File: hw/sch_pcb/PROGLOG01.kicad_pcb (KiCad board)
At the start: 2 copper layers, 60.5 x 40.1 mm, 66 parts, among them J1 JUMP_3X2, J10 HEADER_2x01_PARALLEL, J11 HEADER_2x01_PARALLEL, J13 HEADER_2x01_PARALLEL, J14 HEADER_2x01_PARALLEL, J15 HEADER_2x01_PARALLEL, J16 HEADER_2x01_PARALLEL, J17 HEADER_2x01_PARALLEL, J18 HEADER_2x01_PARALLEL, J19 HEADER_2x01_PARALLEL, J2 HEADER_2x01, J20 HEADER_2x01_PARALLEL, J21 HEADER_2x01_PARALLEL, J22 HEADER_2x01_PARALLEL, J23 HEADER_2x01_PARALLEL, J24 HEADER_2x01_PARALLEL, J25 HEADER_2x01_PARALLEL, J26 SATA, J27 HEADER_2x01_PARALLEL, J28 HEADER_2x01_PARALLEL, J29 HEADER_2x01_PARALLEL, J3 HEADER_2x02_PARALLEL, J30 HEADER_2x01_PARALLEL, J31 HEADER_2x01_PARALLEL, J32 HEADER_2x01_PARALLEL, J33 HEADER_2x01_PARALLEL, J34 HEADER_2x01_PARALLEL, J4 HEADER_2x04, J5 HEADER_2x01_PARALLEL, J6 HEADER_2x01_PARALLEL, J7 HEADER_2x01_PARALLEL, J8 HEADER_2x01_PARALLEL, J9 HEADER_2x01_PARALLEL, M1 HOLE, M2 HOLE, M3 HOLE, M4 HOLE, SW1 SW_Push, U1 TPS22919DCK, U2 MIC5504-1.2YM5, U3 AT25SF081-SSH, U4 ICE40UP5K-SG48I, X1 ISM92-3351AH24.00

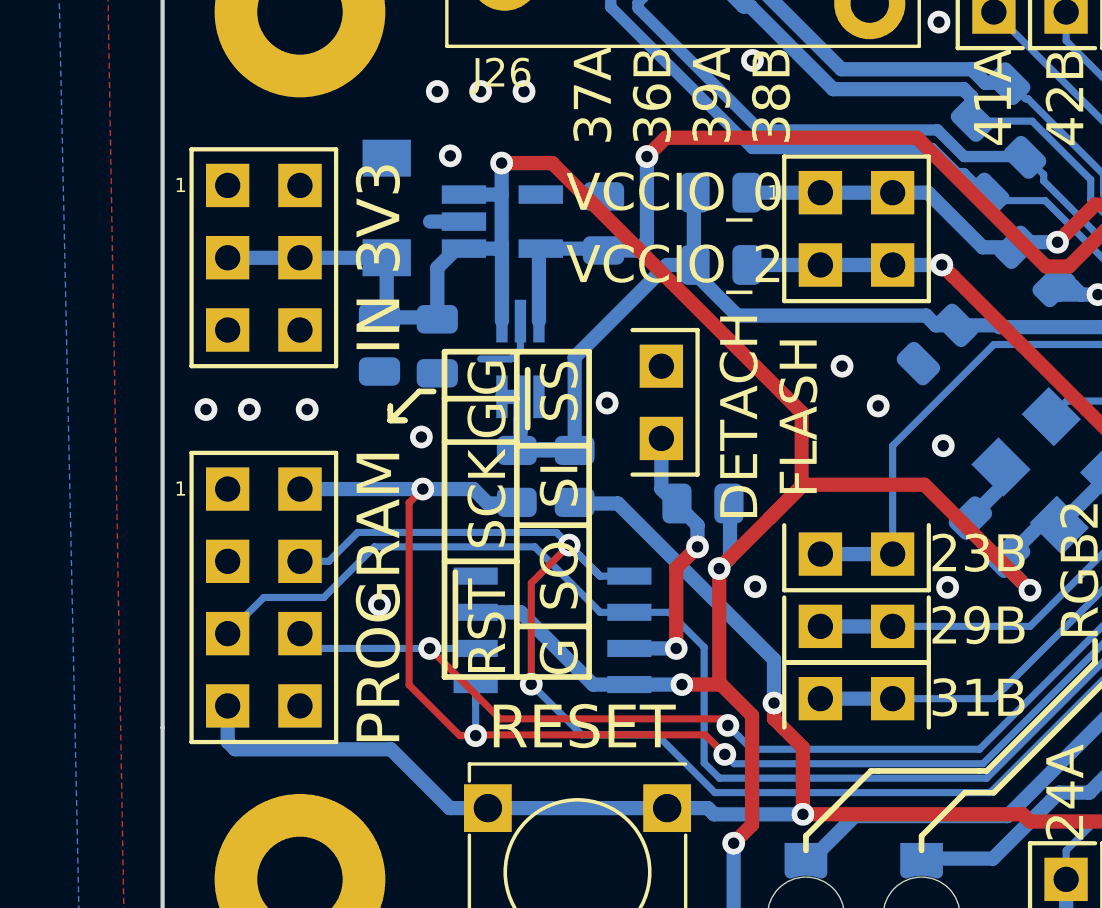
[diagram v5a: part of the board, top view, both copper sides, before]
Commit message: Resolve DRC errors in silkscreen.
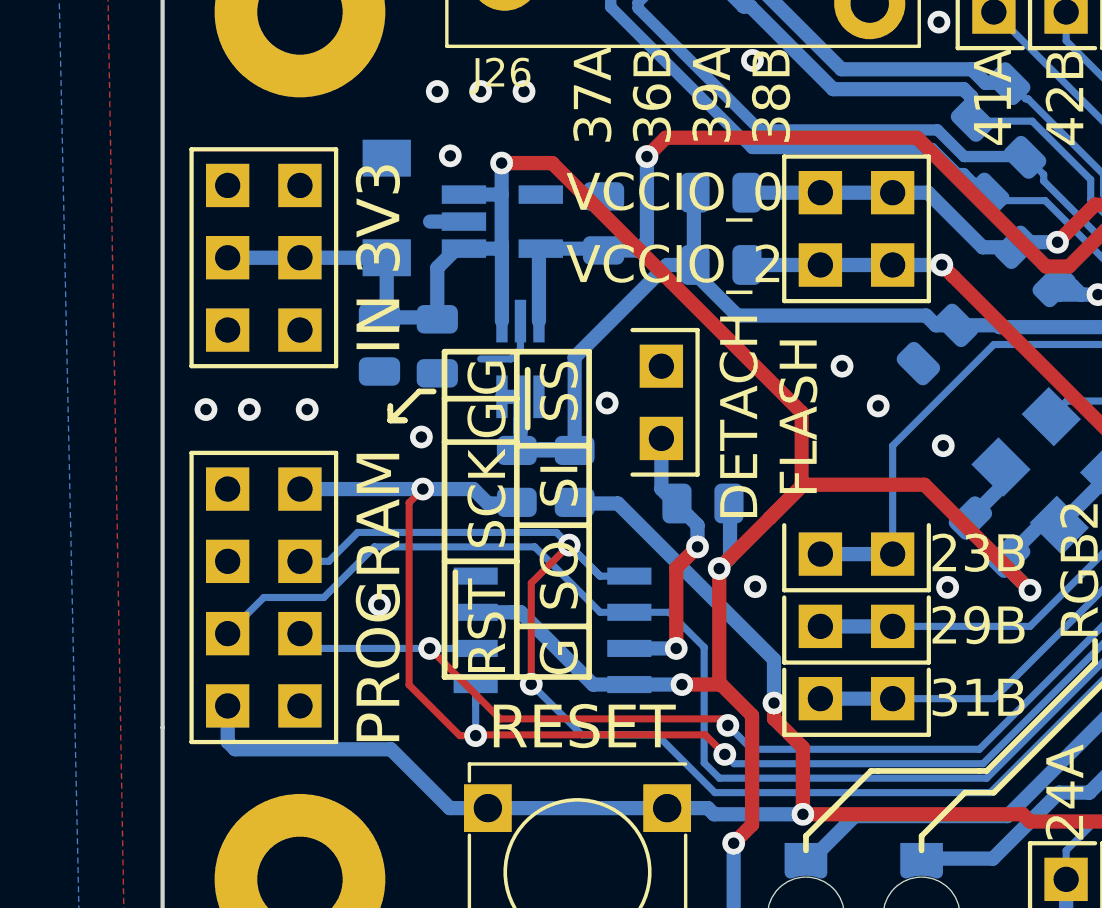
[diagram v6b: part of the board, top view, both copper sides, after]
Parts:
- turned J14 to 0 degrees
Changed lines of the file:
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@@
       (effects (font (size 1.5 1.5) (thickness 0.15)))
-    )
-    (fp_text user "1" (at -2.921 -2.54) (layer "F.SilkS")
-      (effects (font (size 0.5 0.5) (thickness 0.05)))
     )
     (fp_line (start 2.54 -3.81) (end 2.54 3.81) (layer "F.SilkS") (width 0.15))
@@
     (fp_text value "HEADER_2x04" (at 0 6.35) (layer "F.SilkS") hide
       (effects (font (size 1.5 1.5) (thickness 0.15)))
-    )
-    (fp_text user "1" (at -2.921 -3.81) (layer "F.SilkS")
-      (effects (font (size 0.5 0.5) (thickness 0.05)))
     )
     (fp_line (start -2.54 -5.08) (end 2.54 -5.08) (layer "F.SilkS") (width 0.15))
@@
   )
   (footprint "Mlab_Pin_Headers:Straight_2x01" (layer "F.Cu")
-    (at 181.864 130.556 180)
-    (descr "pin header straight 2x01")
-    (tags "pin header straight 2x01")
-    (property "Sheetfile" "PROGLOG01.kicad_sch")
-    (property "Sheetname" "")
-    (attr through_hole)
-    (fp_text reference "J14" (at 0 -2.54 180) (layer "F.SilkS") hide
-      (effects (font (size 1.5 1.5) (thickness 0.15)))
-    )
-    (fp_text value "HEADER_2x01_PARALLEL" (at 0 2.54 180) (layer "F.SilkS") hide
-      (effects (font (size 1.5 1.5) (thickness 0.15)))
-    )
-    (fp_line (start -2.54 1.27) (end -2.54 -1.016) (layer "F.SilkS") (width 0.15))
-    (fp_line (start 2.54 1.27) (end -2.54 1.27) (layer "F.SilkS") (width 0.15))
-    (fp_line (start 2.54 -1.016) (end 2.54 1.27) (layer "F.SilkS") (width 0.15))
-    (fp_line (start 2.54 1.27) (end -2.54 1.27) (layer "F.Fab") (width 0.15))
-    (fp_line (start 2.54 -1.27) (end 2.54 1.27) (layer "F.Fab") (width 0.15))
-    (fp_line (start -2.54 -1.27) (end 2.54 -1.27) (layer "F.Fab") (width 0.15))
-    (fp_line (start -2.54 1.27) (end -2.54 -1.27) (layer "F.Fab") (width 0.15))
-    (pad "1" thru_hole rect (at -1.27 0 180) (size 1.524 1.524) (drill 0.889) (layers *.Cu *.Mask)
+    (at 181.864 130.556)
+    (descr "pin header straight 2x01")
+    (tags "pin header straight 2x01")
+    (property "Sheetfile" "PROGLOG01.kicad_sch")
+    (property "Sheetname" "")
+    (attr through_hole)
+    (fp_text reference "J14" (at 0 -2.54) (layer "F.SilkS") hide
+      (effects (font (size 1.5 1.5) (thickness 0.15)))
+    )
+    (fp_text value "HEADER_2x01_PARALLEL" (at 0 2.54) (layer "F.SilkS") hide
+      (effects (font (size 1.5 1.5) (thickness 0.15)))
+    )
+    (fp_line (start -2.54 1.27) (end -2.54 -1.016) (layer "F.SilkS") (width 0.15))
+    (fp_line (start 2.54 1.27) (end -2.54 1.27) (layer "F.SilkS") (width 0.15))
+    (fp_line (start 2.54 -1.016) (end 2.54 1.27) (layer "F.SilkS") (width 0.15))
+    (fp_line (start 2.54 1.27) (end -2.54 1.27) (layer "F.Fab") (width 0.15))
+    (fp_line (start 2.54 -1.27) (end 2.54 1.27) (layer "F.Fab") (width 0.15))
+    (fp_line (start -2.54 -1.27) (end 2.54 -1.27) (layer "F.Fab") (width 0.15))
+    (fp_line (start -2.54 1.27) (end -2.54 -1.27) (layer "F.Fab") (width 0.15))
+    (pad "1" thru_hole rect (at -1.27 0) (size 1.524 1.524) (drill 0.889) (layers *.Cu *.Mask)
       (net 45 "/IOB_31b") (pintype "input"))
-    (pad "2" thru_hole rect (at 1.27 0 180) (size 1.524 1.524) (drill 0.889) (layers *.Cu *.Mask)
+    (pad "2" thru_hole rect (at 1.27 0) (size 1.524 1.524) (drill 0.889) (layers *.Cu *.Mask)
       (net 45 "/IOB_31b") (pintype "input"))
     (model "${KICAD6_3DMODEL_DIR}/Connector_PinHeader_2.54mm.3dshapes/PinHeader_2x01_P2.54mm_Vertical.wrl"
@@
       (effects (font (size 1.5 1.5) (thickness 0.15)))
     )
-    (fp_text user "1" (at -2.921 -1.27) (layer "F.SilkS")
-      (effects (font (size 0.5 0.5) (thickness 0.05)))
-    )
     (fp_line (start 2.54 2.54) (end -2.54 2.54) (layer "F.SilkS") (width 0.15))

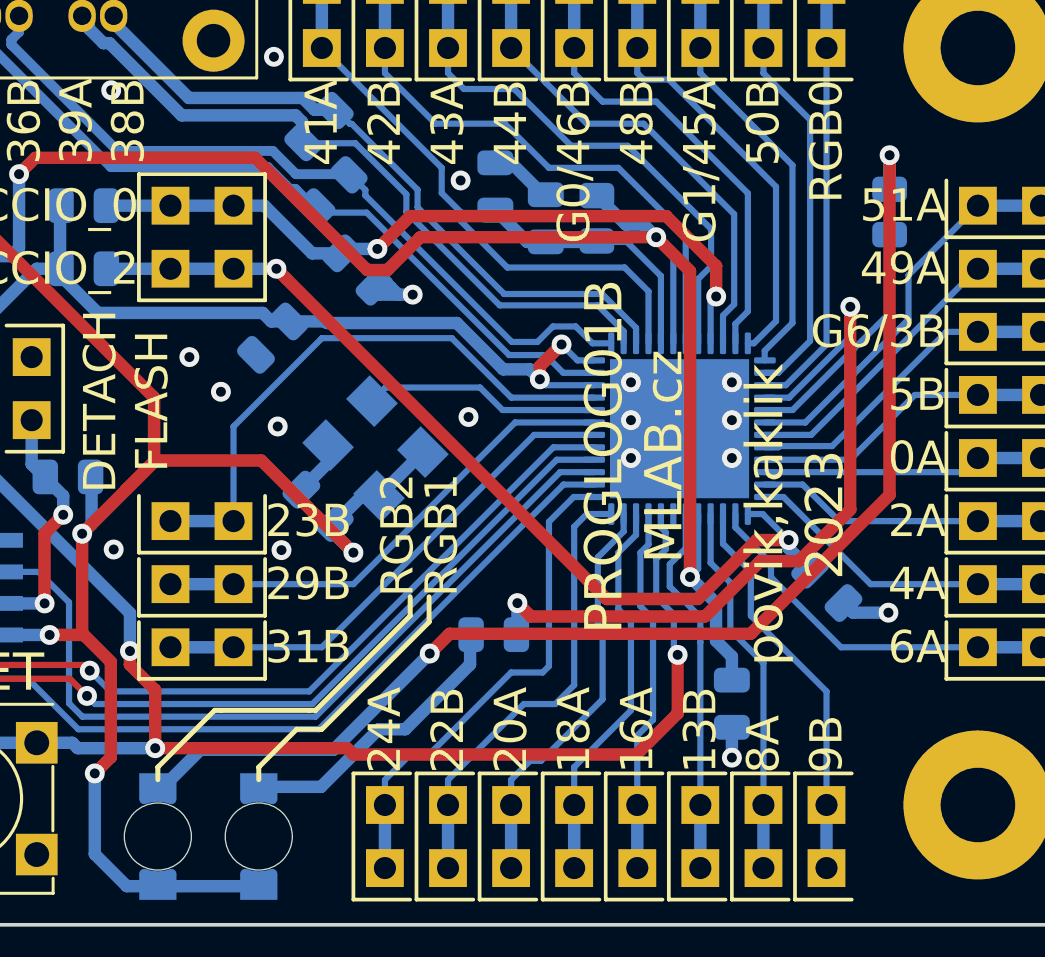
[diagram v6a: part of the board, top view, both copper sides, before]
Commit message: Resolve silkscreen and layout issues.
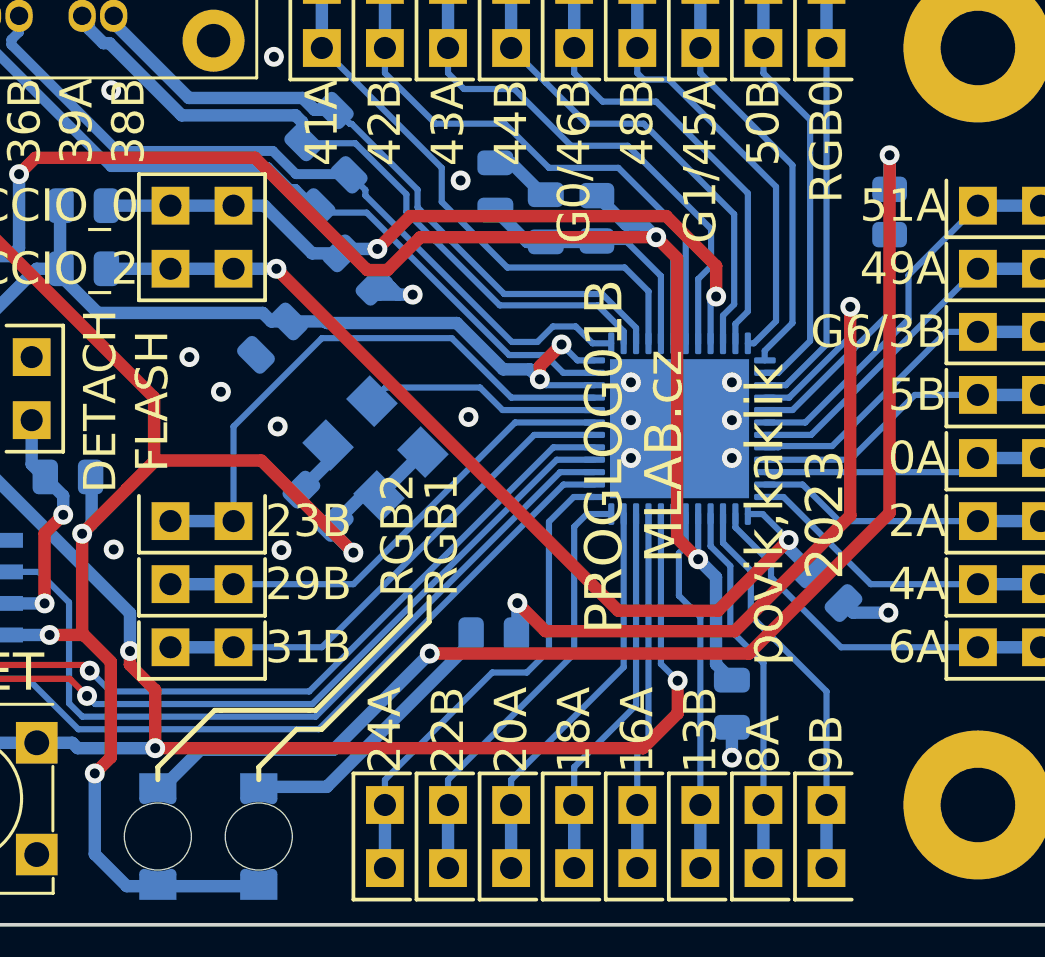
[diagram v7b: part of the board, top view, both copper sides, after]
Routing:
- net +1V2: track 67.2 -> 66.3 mm
- net /IOB_22b: track 18.3 -> 17.5 mm
- net /RGB1: track 30.5 -> 31.1 mm
- net /NRESET: track 68.1 -> 67.6 mm

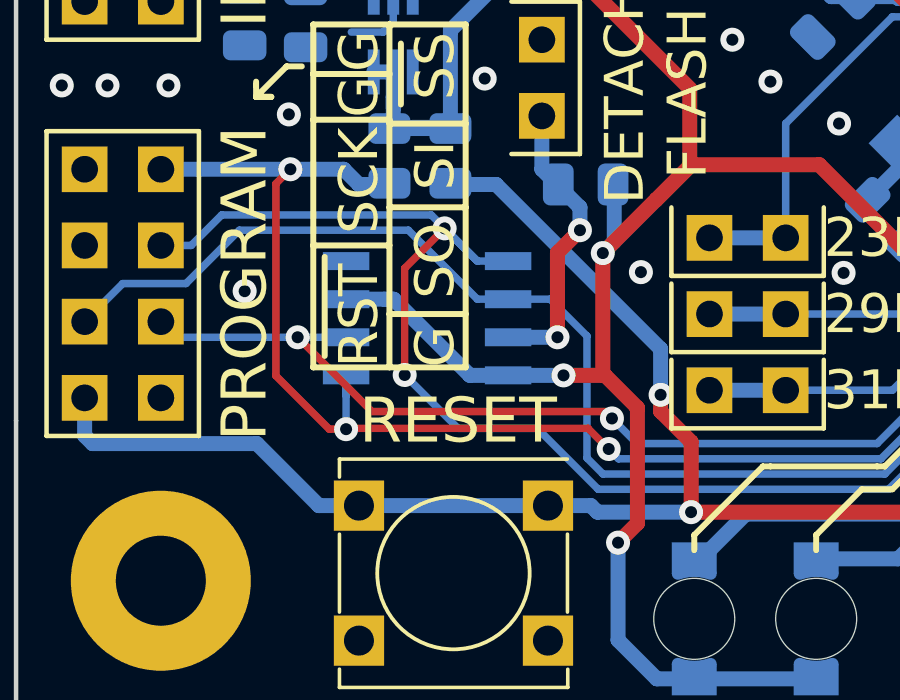
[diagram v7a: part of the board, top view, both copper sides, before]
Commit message: Fix wrong UST_ID assigned.
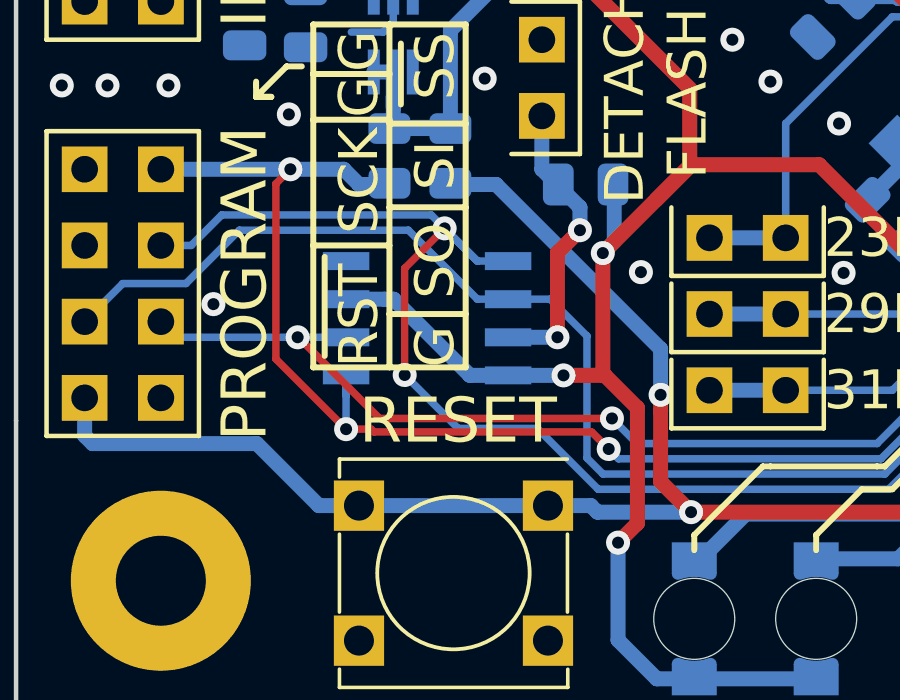
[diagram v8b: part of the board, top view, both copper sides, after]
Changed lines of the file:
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@@
     (property "Sheetfile" "PROGLOG01.kicad_sch")
     (property "Sheetname" "")
-    (property "UST_ID" "5c70984812875079b91f8bc2")
+    (property "UST_ID" "5c70984712875079b91f8b50")
     (attr smd)
     (fp_text reference "C4" (at 0 1.68 270 unlocked) (layer "B.SilkS")
@@
       (effects (font (size 1.524 1.524) (thickness 0.3048)) (justify mirror))
     )
-    (fp_text user "A" (at -1.80086 -1.5494 90) (layer "B.SilkS")
+    (fp_text user "A" (at -1.80086 -1.5494 270 unlocked) (layer "B.SilkS")
       (effects (font (size 0.50038 0.50038) (thickness 0.09906)) (justify mirror))
     )
@@
       (effects (font (size 1.524 1.524) (thickness 0.3048)) (justify mirror))
     )
-    (fp_text user "A" (at -1.80086 -1.5494 90) (layer "B.SilkS")
+    (fp_text user "A" (at -1.80086 -1.5494 270 unlocked) (layer "B.SilkS")
       (effects (font (size 0.50038 0.50038) (thickness 0.09906)) (justify mirror))
     )
@@
   (via (at 199.136 119.888) (size 0.8) (drill 0.4) (layers "F.Cu" "B.Cu") (net 2))
   (via (at 192.5955 121.285) (size 0.8) (drill 0.4) (layers "F.Cu" "B.Cu") (net 2))
-  (via (at 165.1 127.254) (size 0.8) (drill 0.4) (layers "F.Cu" "B.Cu") (net 2))
+  (via (at 164.0586 127.6858) (size 0.8) (drill 0.4) (layers "F.Cu" "B.Cu") (net 2))
   (via (at 178.2064 108.1278) (size 0.8) (drill 0.4) (layers "F.Cu" "B.Cu") (net 2))
   (via (at 209.503219 129.163019) (size 0.8) (drill 0.4) (layers "F.Cu" "B.Cu") (net 2))
@@
   (segment (start 174.498 105.132) (end 174.498 105.782) (width 0.4) (layer "B.Cu") (net 10))
   (segment (start 197.5908 118.3174) (end 196.912399 117.638999) (width 0.25) (layer "B.Cu") (net 10))
-  (segment (start 179.980358 132.275699) (end 178.964358 131.259699) (width 0.5) (layer "F.Cu") (net 11))
   (segment (start 179.980358 134.62) (end 199.61921 134.62) (width 0.5) (layer "F.Cu") (net 11))
+  (segment (start 178.964358 133.604) (end 178.964358 131.259699) (width 0.5) (layer "F.Cu") (net 11))
+  (segment (start 179.980358 134.62) (end 178.964358 133.604) (width 0.5) (layer "F.Cu") (net 11))
   (segment (start 178.961999 131.25734) (end 178.964358 131.259699) (width 0.5) (layer "F.Cu") (net 11))
-  (segment (start 179.980358 134.62) (end 179.980358 132.275699) (width 0.5) (layer "F.Cu") (net 11))
   (segment (start 178.964358 131.259699) (end 178.964357 130.709185) (width 0.5) (layer "F.Cu") (net 11))
   (segment (start 201.0156 133.22361) (end 201.0156 131.9022) (width 0.5) (layer "F.Cu") (net 11))
@@
   (segment (start 167.5714 134.402) (end 168.9096 134.402) (width 0.5) (layer "B.Cu") (net 11))
   (segment (start 159.766 130.81) (end 159.766 132.072) (width 0.5) (layer "B.Cu") (net 11))
-  (segment (start 169.3418 131.2672) (end 177.1142 131.2672) (width 0.25) (layer "F.Cu") (net 12))
-  (segment (start 166.8653 128.7907) (end 169.3418 131.2672) (width 0.25) (layer "F.Cu") (net 12))
-  (segment (start 177.1142 131.2672) (end 177.3428 131.4958) (width 0.25) (layer "F.Cu") (net 12))
+  (segment (start 166.8653 128.7907) (end 166.89139 128.7907) (width 0.25) (layer "F.Cu") (net 12))
+  (segment (start 169.59649 131.4958) (end 177.3428 131.4958) (width 0.25) (layer "F.Cu") (net 12))
+  (segment (start 166.89139 128.7907) (end 169.59649 131.4958) (width 0.25) (layer "F.Cu") (net 12))
   (via (at 166.8653 128.7907) (size 0.8) (drill 0.4) (layers "F.Cu" "B.Cu") (net 12))
   (via (at 177.3428 131.4958) (size 0.8) (drill 0.4) (layers "F.Cu" "B.Cu") (net 12))
@@
   (segment (start 170.55706 125.222) (end 164.923002 125.222) (width 0.25) (layer "B.Cu") (net 13))
   (segment (start 163.145002 127) (end 161.036 127) (width 0.25) (layer "B.Cu") (net 13))
+  (segment (start 176.665129 131.945301) (end 169.410301 131.945301) (width 0.25) (layer "F.Cu") (net 14))
+  (segment (start 166.1408 123.6732) (end 166.1408 129.514) (width 0.25) (layer "F.Cu") (net 14))
+  (segment (start 169.3164 131.8514) (end 168.48332 131.8514) (width 0.25) (layer "F.Cu") (net 14))
+  (segment (start 177.234664 132.514836) (end 176.665129 131.945301) (width 0.25) (layer "F.Cu") (net 14))
+  (segment (start 166.1408 129.514) (end 168.48076 131.85396) (width 0.25) (layer "F.Cu") (net 14))
   (segment (start 166.624 123.19) (end 166.1408 123.6732) (width 0.25) (layer "F.Cu") (net 14))
-  (segment (start 166.1408 130.0728) (end 167.92196 131.85396) (width 0.25) (layer "F.Cu") (net 14))
-  (segment (start 168.48076 131.85396) (end 168.50872 131.826) (width 0.25) (layer "F.Cu") (net 14))
-  (segment (start 176.545828 131.826) (end 177.234664 132.514836) (width 0.25) (layer "F.Cu") (net 14))
-  (segment (start 168.50872 131.826) (end 176.545828 131.826) (width 0.25) (layer "F.Cu") (net 14))
-  (segment (start 166.1408 123.6732) (end 166.1408 130.0728) (width 0.25) (layer "F.Cu") (net 14))
-  (segment (start 167.92196 131.85396) (end 168.48076 131.85396) (width 0.25) (layer "F.Cu") (net 14))
+  (segment (start 168.48332 131.8514) (end 168.48076 131.85396) (width 0.25) (layer "F.Cu") (net 14))
+  (segment (start 169.410301 131.945301) (end 169.3164 131.8514) (width 0.25) (layer "F.Cu") (net 14))
   (via (at 166.624 123.19) (size 0.8) (drill 0.4) (layers "F.Cu" "B.Cu") (net 14))
   (via (at 168.48076 131.85396) (size 0.8) (drill 0.4) (layers "F.Cu" "B.Cu") (net 14))
